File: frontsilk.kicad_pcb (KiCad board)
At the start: 2 copper layers, 0 parts

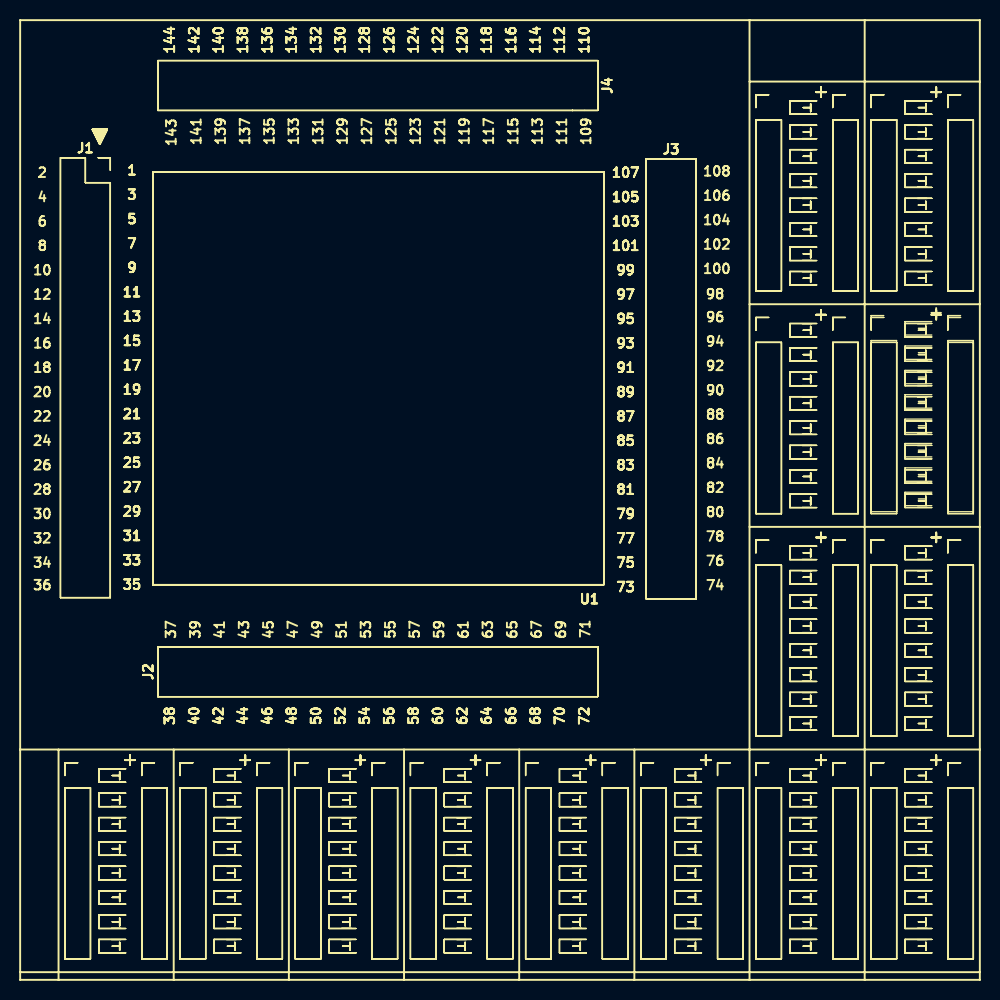
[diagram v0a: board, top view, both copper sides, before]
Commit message: changed as the IC51-socket edge cut
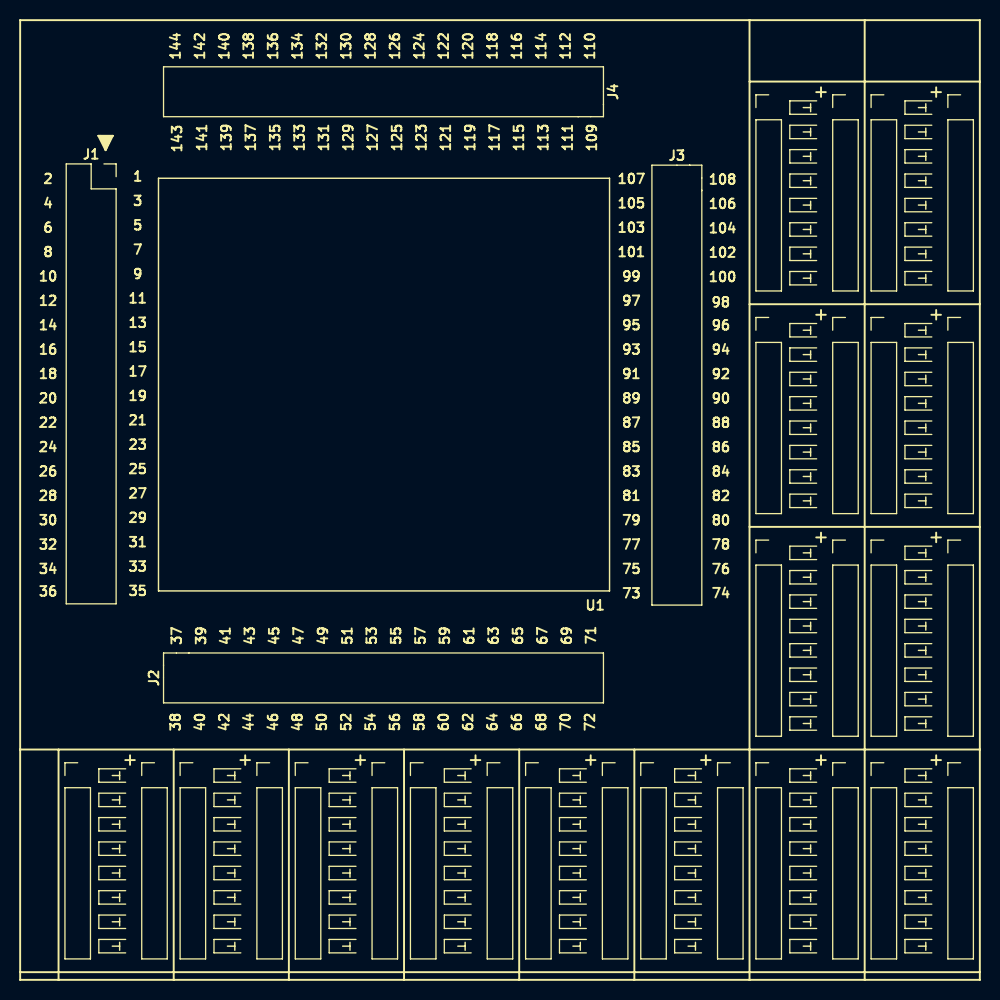
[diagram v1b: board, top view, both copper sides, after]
